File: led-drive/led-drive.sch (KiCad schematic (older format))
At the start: 24 parts, among them IC1 TPS92512, P1 PWR_CONN, P2 CTRL, P3 LED, Q1 Q_PMOS_GDS, U1 TS881

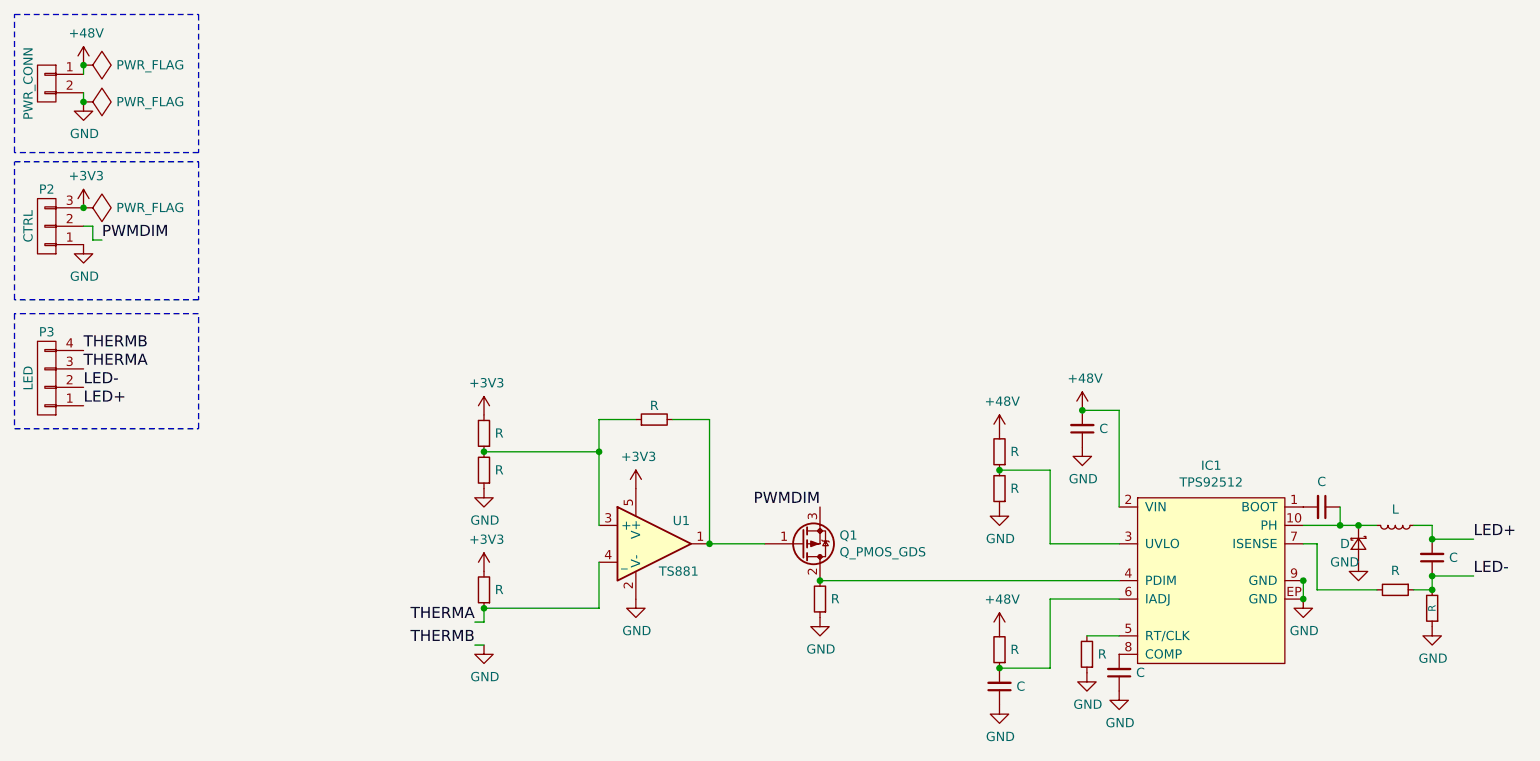
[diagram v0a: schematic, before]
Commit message: Component values for TPS
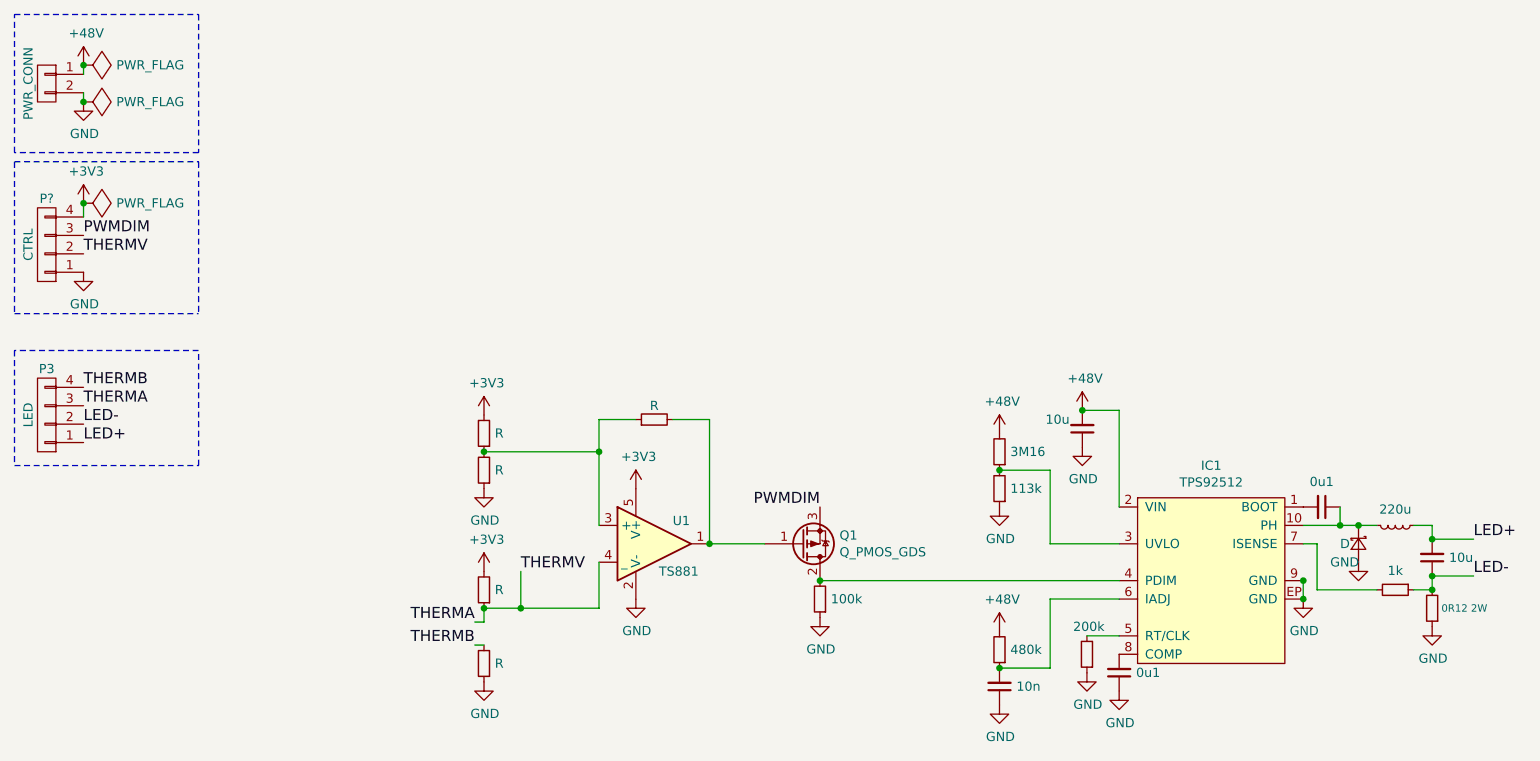
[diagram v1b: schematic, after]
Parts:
- removed P2: CTRL, symbol CONN_01X03
- added P?: CTRL, symbol CONN_01X04
- added R?: R, symbol R_Small
- C1: value C -> 10n
- C2, C5: value C -> 10u
- C3, C4: value C -> 0u1
- L1: value L -> 220u
- R10: value R -> 1k
- R11: value R -> 0R12 2W
- R5: value R -> 100k
- R6: value R -> 3M16
- R7: value R -> 113k
- R8: value R -> 480k
- R9: value R -> 200k
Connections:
- net +3V3: now also P?.4 (P4)
- net GND: now also P?.1 (P1), R?.1; no longer P3.4 (P4)
- net PWMDIM: now also P?.3 (P3)
- net THERMA: now also P?.2 (P2)
- new net THERMB: P3.4 (P4), R?.2
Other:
- moved on the sheet: P3
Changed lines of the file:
@@
 P 8050 3300
 F 0 "L1" V 7872 3300 50  0001 C CNN
-F 1 "L" V 7963 3300 50  0000 C CNN
+F 1 "220u" V 7963 3300 50  0000 C CNN
 F 2 "" H 8050 3300 50  0000 C CNN
 F 3 "" H 8050 3300 50  0000 C CNN
@@
 P 7650 3200
 F 0 "C4" V 7421 3200 50  0001 C CNN
-F 1 "C" V 7513 3200 50  0000 C CNN
+F 1 "0u1" V 7513 3200 50  0000 C CNN
 F 2 "" H 7650 3200 50  0000 C CNN
 F 3 "" H 7650 3200 50  0000 C CNN
@@
 P 8050 3650
 F 0 "R10" H 8109 3696 50  0001 L CNN
-F 1 "R" V 7946 3650 50  0000 C CNN
+F 1 "1k" V 7946 3650 50  0000 C CNN
 F 2 "" H 8050 3650 50  0000 C CNN
 F 3 "" H 8050 3650 50  0000 C CNN
@@
 P 8250 3475
 F 0 "C5" V 8021 3475 50  0001 C CNN
-F 1 "C" H 8158 3475 50  0000 R CNN
+F 1 "10u" H 8158 3475 50  0000 R CNN
 F 2 "" H 8250 3475 50  0000 C CNN
 F 3 "" H 8250 3475 50  0000 C CNN
@@
 P 8250 3750
 F 0 "R11" H 8309 3796 50  0001 L CNN
-F 1 "R" V 8250 3750 40  0000 C CNN
+F 1 "0R12 2W" H 8075 3750 40  0000 C CNN
 F 2 "" H 8250 3750 50  0000 C CNN
 F 3 "" H 8250 3750 50  0000 C CNN
@@
 P 6550 4100
 F 0 "C3" V 6321 4100 50  0001 C CNN
-F 1 "C" H 6458 4100 50  0000 R CNN
+F 1 "0u1" H 6458 4100 50  0000 R CNN
 F 2 "" H 6550 4100 50  0000 C CNN
 F 3 "" H 6550 4100 50  0000 C CNN
@@
 P 5900 2900
 F 0 "R6" H 5959 2946 50  0001 L CNN
-F 1 "R" H 5841 2900 50  0000 R CNN
+F 1 "3M16" H 5841 2900 50  0000 R CNN
 F 2 "" H 5900 2900 50  0000 C CNN
 F 3 "" H 5900 2900 50  0000 C CNN
@@
 P 5900 3100
 F 0 "R7" H 5959 3146 50  0001 L CNN
-F 1 "R" H 5841 3100 50  0000 R CNN
+F 1 "113k" H 5841 3100 50  0000 R CNN
 F 2 "" H 5900 3100 50  0000 C CNN
 F 3 "" H 5900 3100 50  0000 C CNN
@@
 P 5900 3975
 F 0 "R8" H 5959 4021 50  0001 L CNN
-F 1 "R" H 5841 3975 50  0000 R CNN
+F 1 "480k" H 5841 3975 50  0000 R CNN
 F 2 "" H 5900 3975 50  0000 C CNN
 F 3 "" H 5900 3975 50  0000 C CNN
@@
 P 5900 4175
 F 0 "C1" V 5671 4175 50  0001 C CNN
-F 1 "C" H 5808 4175 50  0000 R CNN
+F 1 "10n" H 5808 4175 50  0000 R CNN
 F 2 "" H 5900 4175 50  0000 C CNN
 F 3 "" H 5900 4175 50  0000 C CNN
@@
 P 6375 4000
 F 0 "R9" H 6434 4046 50  0001 L CNN
-F 1 "R" H 6316 4000 50  0000 R CNN
+F 1 "200k" H 6450 3850 50  0000 R CNN
 F 2 "" H 6375 4000 50  0000 C CNN
 F 3 "" H 6375 4000 50  0000 C CNN
@@
 P 6350 2775
 F 0 "C2" V 6121 2775 50  0001 C CNN
-F 1 "C" H 6258 2775 50  0000 R CNN
+F 1 "10u" H 6550 2725 50  0000 R CNN
 F 2 "" H 6350 2775 50  0000 C CNN
 F 3 "" H 6350 2775 50  0000 C CNN
@@
 L GND #PWR014
 U 1 1 584FD8FA
-P 925 1775
-F 0 "#PWR014" H 925 1525 50  0001 C CNN
-F 1 "GND" H 930 1602 50  0000 C CNN
-F 2 "" H 925 1775 50  0000 C CNN
-F 3 "" H 925 1775 50  0000 C CNN
-	1    925  1775
+P 925 1925
+F 0 "#PWR014" H 925 1675 50  0001 C CNN
+F 1 "GND" H 930 1752 50  0000 C CNN
+F 2 "" H 925 1925 50  0000 C CNN
+F 3 "" H 925 1925 50  0000 C CNN
+	1    925  1925
 	1    0    0    -1
 $EndComp
@@
 	550  1325 1550 1325
 Wire Notes Line
-	1550 1325 1550 2075
-Wire Notes Line
-	1550 2075 550  2075
-Wire Notes Line
-	550  2075 550  1325
-Text Label 1025 1750 0    60   ~ 0
+	1550 1325 1550 2150
+Wire Notes Line
+	550  1325 550  2150
+Text Label 925  1725 0    60   ~ 0
 PWMDIM
 Wire Wire Line
@@
 L CONN_01X04 P3
 U 1 1 584FDC1F
-P 725 2500
-F 0 "P3" H 725 2250 50  0000 C CNN
-F 1 "LED" V 825 2500 50  0000 C CNN
-F 2 "" H 725 2500 50  0000 C CNN
-F 3 "" H 725 2500 50  0000 C CNN
-	1    725  2500
-	-1   0    0    1
-$EndComp
+P 725 2700
+F 0 "P3" H 725 2450 50  0000 C CNN
+F 1 "LED" V 825 2700 50  0000 C CNN
+F 2 "" H 725 2700 50  0000 C CNN
+F 3 "" H 725 2700 50  0000 C CNN
+	1    725  2700
+	-1   0    0    1
+$EndComp
+Text Label 925  2850 0    60   ~ 0
+LED+
+Text Label 925  2750 0    60   ~ 0
+LED-
 Text Label 925  2650 0    60   ~ 0
-LED+
+THERMA
 Text Label 925  2550 0    60   ~ 0
-LED-
-Text Label 925  2450 0    60   ~ 0
-THERMA
-Text Label 925  2350 0    60   ~ 0
 THERMB
 $Comp
@@
 L GND #PWR017
 U 1 1 584FE126
-P 3100 3950
-F 0 "#PWR017" H 3100 3700 50  0001 C CNN
-F 1 "GND" H 3105 3777 50  0000 C CNN
-F 2 "" H 3100 3950 50  0000 C CNN
-F 3 "" H 3100 3950 50  0000 C CNN
-	1    3100 3950
+P 3100 4150
+F 0 "#PWR017" H 3100 3900 50  0001 C CNN
+F 1 "GND" H 3105 3977 50  0000 C CNN
+F 2 "" H 3100 4150 50  0000 C CNN
+F 3 "" H 3100 4150 50  0000 C CNN
+	1    3100 4150
 	1    0    0    -1
 $EndComp
@@
 	3725 3750 3725 3500
 Wire Notes Line
-	1550 2150 550  2150
-Wire Notes Line
-	550  2150 550  2775
-Wire Notes Line
-	550  2775 1550 2775
-Wire Notes Line
-	1550 2775 1550 2150
-$Comp
-L CONN_01X03 P2
-U 1 1 584FFAC3
-P 725 1675
-F 0 "P2" H 725 1475 50  0000 C CNN
-F 1 "CTRL" V 825 1675 50  0000 C CNN
-F 2 "" H 725 1675 50  0000 C CNN
-F 3 "" H 725 1675 50  0000 C CNN
-	1    725  1675
-	-1   0    0    1
-$EndComp
+	1550 2350 550  2350
+Wire Notes Line
+	550  2350 550  2975
+Wire Notes Line
+	550  2975 1550 2975
+Wire Notes Line
+	1550 2975 1550 2350
 $Comp
 L +3V3 #PWR020
 U 1 1 584FFCBA
-P 925 1575
-F 0 "#PWR020" H 925 1425 50  0001 C CNN
-F 1 "+3V3" H 940 1748 50  0000 C CNN
-F 2 "" H 925 1575 50  0000 C CNN
-F 3 "" H 925 1575 50  0000 C CNN
-	1    925  1575
+P 925 1550
+F 0 "#PWR020" H 925 1400 50  0001 C CNN
+F 1 "+3V3" H 940 1723 50  0000 C CNN
+F 2 "" H 925 1550 50  0000 C CNN
+F 3 "" H 925 1550 50  0000 C CNN
+	1    925  1550
 	1    0    0    -1
 $EndComp
@@
 P 4925 3700
 F 0 "R5" H 4984 3746 50  0001 L CNN
-F 1 "R" H 4866 3700 50  0000 R CNN
+F 1 "100k" H 4866 3700 50  0000 R CNN
 F 2 "" H 4925 3700 50  0000 C CNN
 F 3 "" H 4925 3700 50  0000 C CNN
@@
 L PWR_FLAG #FLG025
 U 1 1 58500834
-P 925 1575
-F 0 "#FLG025" H 925 1670 50  0001 C CNN
-F 1 "PWR_FLAG" V 925 1753 50  0000 L CNN
-F 2 "" H 925 1575 50  0000 C CNN
-F 3 "" H 925 1575 50  0000 C CNN
-	1    925  1575
+P 925 1550
+F 0 "#FLG025" H 925 1645 50  0001 C CNN
+F 1 "PWR_FLAG" V 925 1728 50  0000 L CNN
+F 2 "" H 925 1550 50  0000 C CNN
+F 3 "" H 925 1550 50  0000 C CNN
+	1    925  1550
 	0    1    1    0
 $EndComp
-Wire Wire Line
-	1025 1750 975  1750
-Wire Wire Line
-	975  1750 975  1675
-Wire Wire Line
-	975  1675 925  1675
-Connection ~ 925  1575
+$Comp
+L CONN_01X04 P?
+U 1 1 5852B5A7
+P 725 1775
+F 0 "P?" H 725 1525 50  0000 C CNN
+F 1 "CTRL" V 825 1775 50  0000 C CNN
+F 2 "" H 725 1775 50  0000 C CNN
+F 3 "" H 725 1775 50  0000 C CNN
+	1    725  1775
+	-1   0    0    1
+$EndComp
+Text Label 925  1825 0    60   ~ 0
+THERMV
+Wire Notes Line
+	550  2150 1550 2150
+Wire Wire Line
+	925  1550 925  1625
+Connection ~ 925  1550
+Text Label 3300 3550 0    60   ~ 0
+THERMV
+Wire Wire Line
+	3300 3550 3300 3750
+Connection ~ 3300 3750
+$Comp
+L R_Small R?
+U 1 1 5852BF1D
+P 3100 4050
+F 0 "R?" H 3159 4096 50  0001 L CNN
+F 1 "R" H 3041 4050 50  0000 R CNN
+F 2 "" H 3100 4050 50  0000 C CNN
+F 3 "" H 3100 4050 50  0000 C CNN
+	1    3100 4050
+	-1   0    0    1
+$EndComp
 $EndSCHEMATC
